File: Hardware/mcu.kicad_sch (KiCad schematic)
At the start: 20 parts, among them J1 I2C Debug, J2 Screen, J3 SPI Debug, SW1 TRIGGER, SW2 RESET, U6 ESP32-DevKitC

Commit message: Version 0.1
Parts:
- removed B1: Button, Connector_JST:JST_SH_BM04B-SRSS-TB_1x04-1MP_P1.00mm_Vertical, symbol Connector_Generic:Conn_01x03
- removed C19, C20: 104, Capacitor_SMD:C_0805_2012Metric_Pad1.18x1.45mm_HandSolder, symbol Device:C
- removed CH1: Power, Connector_JST:JST_XH_B2B-XH-A_1x02_P2.50mm_Vertical, symbol Connector_Generic:Conn_01x02
- removed D12, D2: WS2812B, LED_SMD:LED_WS2812B_PLCC4_5.0x5.0mm_P3.2mm, symbol LED:WS2812B
- removed D3: POWER LED, LED_SMD:LED_0805_2012Metric_Pad1.15x1.40mm_HandSolder, symbol Device:LED
- removed J1: I2C Debug, Connector_JST:JST_XH_B4B-XH-A_1x04_P2.50mm_Vertical, symbol Connector_Generic:Conn_01x04
- removed J2: Screen, Connector_JST:JST_XH_S8B-XH-A_1x08_P2.50mm_Horizontal, symbol Connector_Generic:Conn_01x08
- removed J3: SPI Debug, Connector_JST:JST_XH_B4B-XH-A_1x04_P2.50mm_Vertical, symbol Connector_Generic:Conn_01x04
- removed JP1: SolderJumper_2_Open, Jumper:SolderJumper-2_P1.3mm_Open_TrianglePad1.0x1.5mm, symbol Jumper:SolderJumper_2_Open
- removed JP2, JP3: SolderJumper_3_Open, Jumper:SolderJumper-3_P2.0mm_Open_TrianglePad1.0x1.5mm_NumberLabels, symbol Jumper:SolderJumper_3_Open
- removed R16: 170, Resistor_SMD:R_0805_2012Metric_Pad1.20x1.40mm_HandSolder, symbol Device:R
- removed R17: 150, Resistor_SMD:R_0805_2012Metric_Pad1.20x1.40mm_HandSolder, symbol Device:R
- removed R18, R19: 10k, Resistor_SMD:R_0805_2012Metric_Pad1.20x1.40mm_HandSolder, symbol Device:R
- removed SW1: TRIGGER, Button_Switch_THT:SW_PUSH_6mm, symbol Switch:SW_Push
- removed SW2: RESET, Button_Switch_THT:SW_PUSH_6mm, symbol Switch:SW_Push
- removed U6: ESP32-DevKitC, ESP32:ESP32-DevKitC, symbol Espressif:ESP32-DevKitC
- added D3: (no value), symbol Everlight-EAHC2835WD6:EAHC2835WD6
- added Q1: (no value), symbol Diodes_Inc._-_BSS138DW-7-F:BSS138DW-7-F
- added R10, R7, R8, R9: 10k, symbol Device:R
- added U6: (no value), symbol AS7341-DLGT:AS7341-DLGT
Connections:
- net +3V3: now also D3.1 (CATHODE), R10.1, R9.1
- net GND: now also U6.3 (GND)
- net SCL: now also Q1.6 (D2), R9.2
- net SDA: now also Q1.3 (D1), R10.2
- new net: D3.2 (ANODE), U6.4 (LDR)
- new net +1V8: Q1.2 (G2), Q1.5 (G1), R7.1, R8.1, U6.1 (VDD)
- new net SCL_2v: Q1.1 (S2), R7.2, U6.2 (SCL)
- new net SDA_2v: Q1.4 (S1), R8.2, U6.8 (SDA)
- no-connect marks 15 -> 0
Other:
- note removed: "Buttons"
- note removed: "Connectors"
- note removed: "LEDs"

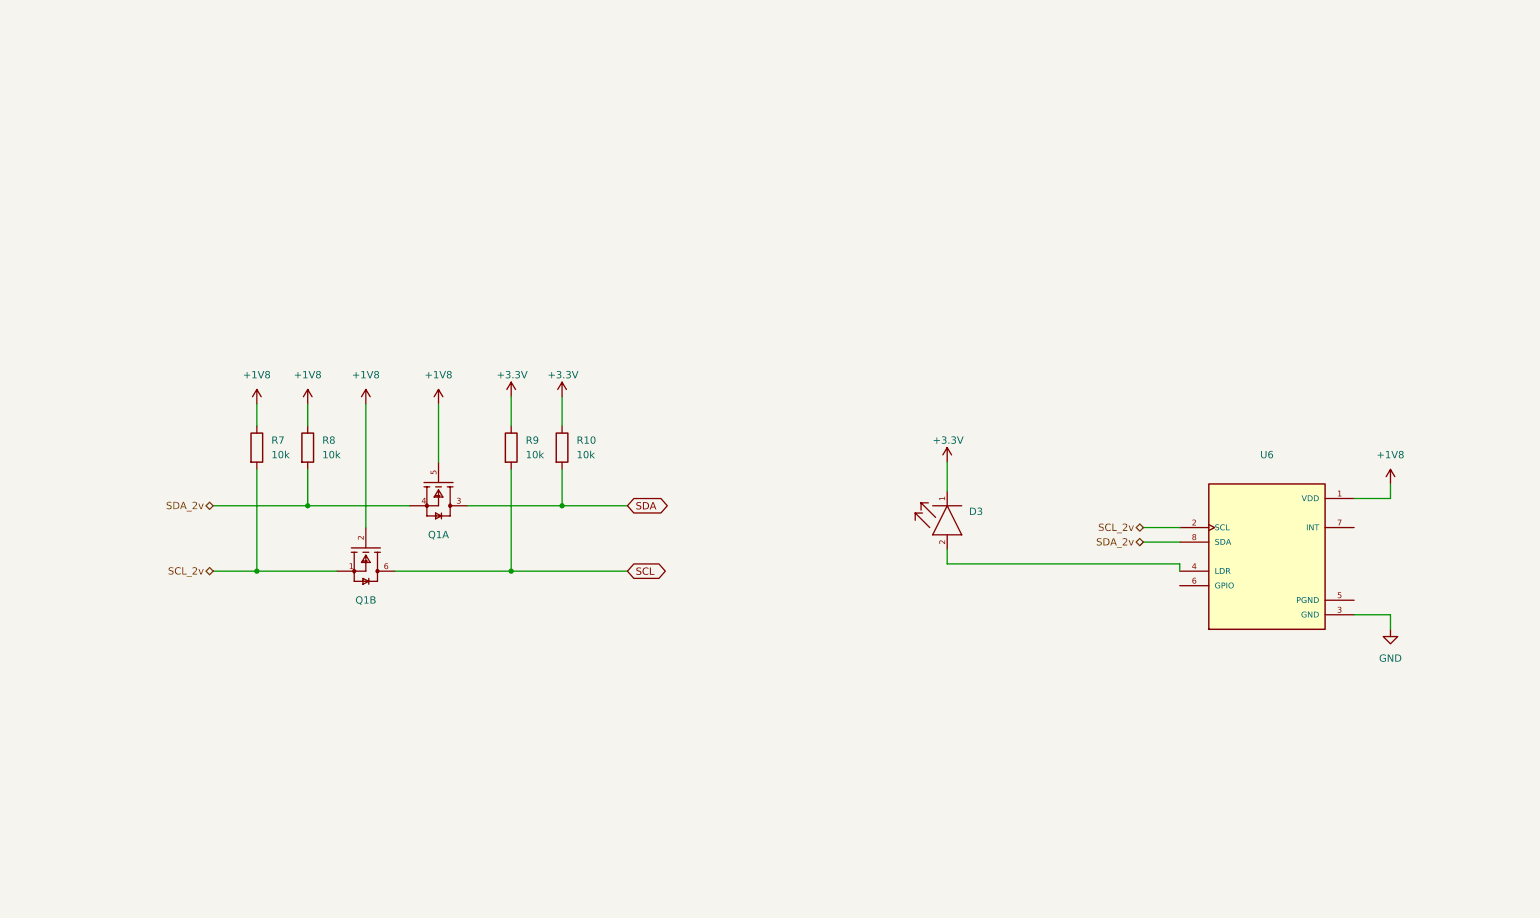
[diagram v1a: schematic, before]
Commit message: Readme + hole update
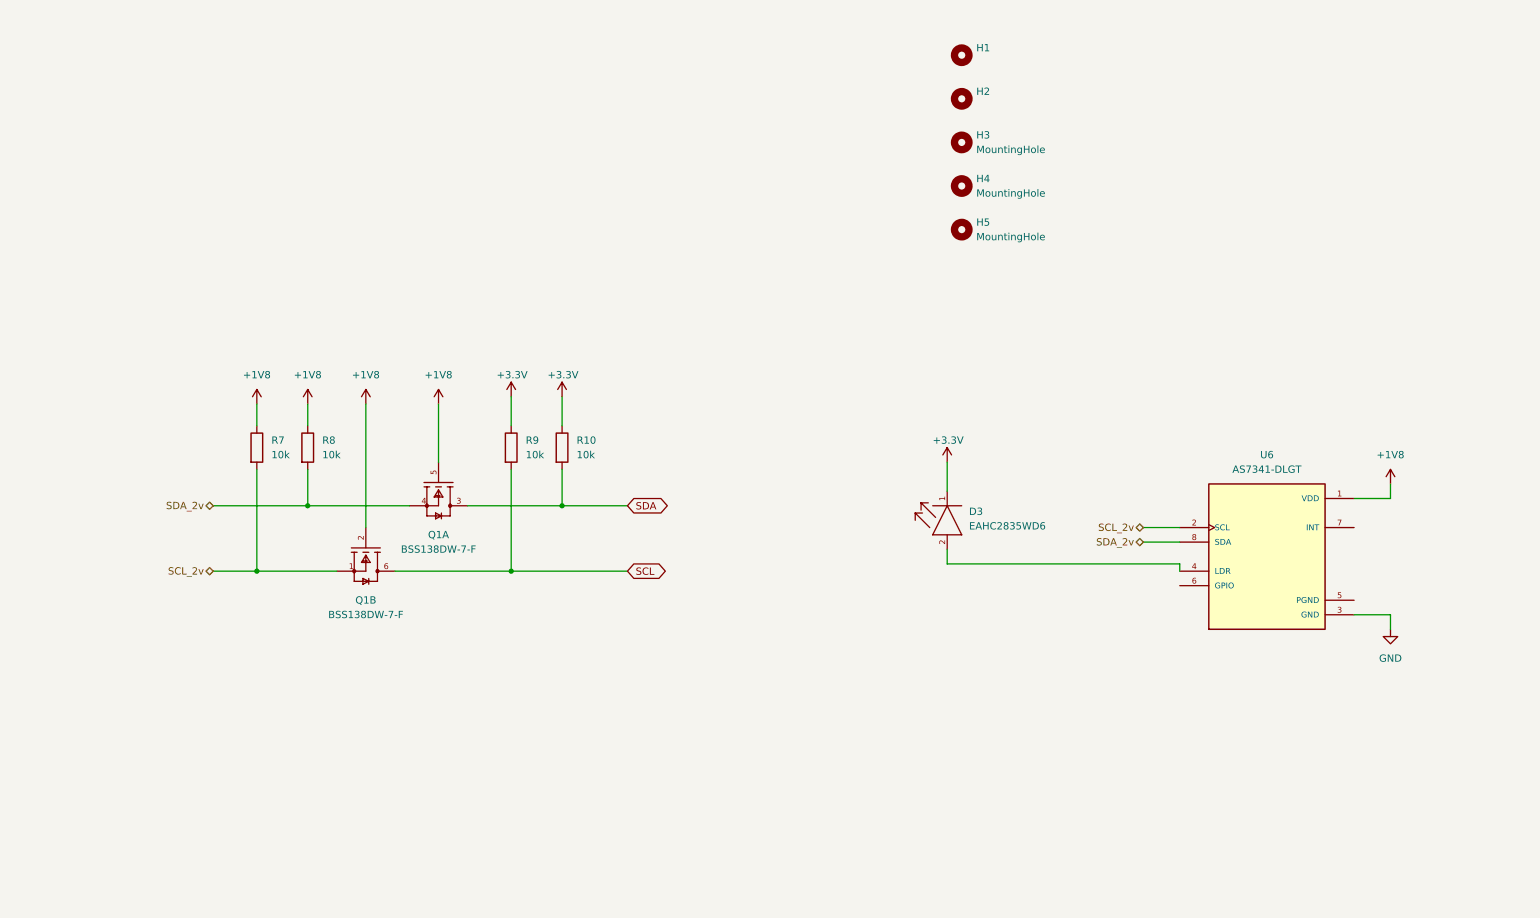
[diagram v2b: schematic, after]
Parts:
- added H1, H2: (no value), symbol Mechanical:MountingHole
- added H3, H4, H5: MountingHole, symbol Mechanical:MountingHole
- D3: value (none) -> EAHC2835WD6; footprint (none) -> Everlight-EAHC2835WD6:Everlight-EAHC2835WD6-MFG
- Q1: value (none) -> BSS138DW-7-F; footprint (none) -> BSS138DW-7-F-A:Diodes_Inc._-_BSS138DW-7-F-A
- R10, R7, R8, R9: footprint (none) -> Resistor_SMD:R_0603_1608Metric_Pad0.98x0.95mm_HandSolder
- U6: value (none) -> AS7341-DLGT; footprint (none) -> AS7341-DLGT:PSON80P310X200X110-8N
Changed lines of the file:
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@@
       (effects (font (size 1.27 1.27)) (justify left))
     )
-    (property "Footprint" "" (id 2) (at 66.802 100.33 90)
+    (property "Footprint" "Resistor_SMD:R_0603_1608Metric_Pad0.98x0.95mm_HandSolder" (id 2) (at 66.802 100.33 90)
       (effects (font (size 1.27 1.27)) hide)
     )
@@
     (pin "1")
   )
+  (symbol (lib_id "Mechanical:MountingHole") (at 182.88 39.37 0) (unit 1)
+    (in_bom yes) (on_board yes) (fields_autoplaced)
+    (property "Reference" "H2" (id 0) (at 185.42 38.0999 0)
+      (effects (font (size 1.27 1.27)) (justify left))
+    )
+    (property "Value" "" (id 1) (at 185.42 40.6399 0)
+      (effects (font (size 1.27 1.27)) (justify left))
+    )
+    (property "Footprint" "" (id 2) (at 182.88 39.37 0)
+      (effects (font (size 1.27 1.27)) hide)
+    )
+    (property "Datasheet" "~" (id 3) (at 182.88 39.37 0)
+      (effects (font (size 1.27 1.27)) hide)
+    )
+  )
   (symbol (lib_id "Everlight-EAHC2835WD6:EAHC2835WD6") (at 180.34 120.65 90) (unit 1)
     (in_bom yes) (on_board yes) (fields_autoplaced)
@@
       (effects (font (size 1.27 1.27)) (justify right))
     )
-    (property "Value" "" (id 1) (at 184.15 114.0459 90)
+    (property "Value" "EAHC2835WD6" (id 1) (at 184.15 114.0459 90)
       (effects (font (size 1.27 1.27)) (justify right))
     )
-    (property "Footprint" "" (id 2) (at 165.1 120.65 0)
+    (property "Footprint" "Everlight-EAHC2835WD6:Everlight-EAHC2835WD6-MFG" (id 2) (at 165.1 120.65 0)
       (effects (font (size 1.27 1.27)) (justify left) hide)
     )
@@
     (pin "2")
   )
+  (symbol (lib_id "Mechanical:MountingHole") (at 182.88 62.23 0) (unit 1)
+    (in_bom yes) (on_board yes) (fields_autoplaced)
+    (property "Reference" "H5" (id 0) (at 185.42 60.9599 0)
+      (effects (font (size 1.27 1.27)) (justify left))
+    )
+    (property "Value" "MountingHole" (id 1) (at 185.42 63.4999 0)
+      (effects (font (size 1.27 1.27)) (justify left))
+    )
+    (property "Footprint" "" (id 2) (at 182.88 62.23 0)
+      (effects (font (size 1.27 1.27)) hide)
+    )
+    (property "Datasheet" "~" (id 3) (at 182.88 62.23 0)
+      (effects (font (size 1.27 1.27)) hide)
+    )
+  )
   (symbol (lib_id "Device:R") (at 104.14 100.33 0) (unit 1)
     (in_bom yes) (on_board yes) (fields_autoplaced)
@@
       (effects (font (size 1.27 1.27)) (justify left))
     )
-    (property "Footprint" "" (id 2) (at 102.362 100.33 90)
+    (property "Footprint" "Resistor_SMD:R_0603_1608Metric_Pad0.98x0.95mm_HandSolder" (id 2) (at 102.362 100.33 90)
       (effects (font (size 1.27 1.27)) hide)
     )
@@
     (pin "1")
   )
+  (symbol (lib_id "Mechanical:MountingHole") (at 182.88 46.99 0) (unit 1)
+    (in_bom yes) (on_board yes) (fields_autoplaced)
+    (property "Reference" "H3" (id 0) (at 185.42 45.7199 0)
+      (effects (font (size 1.27 1.27)) (justify left))
+    )
+    (property "Value" "MountingHole" (id 1) (at 185.42 48.2599 0)
+      (effects (font (size 1.27 1.27)) (justify left))
+    )
+    (property "Footprint" "" (id 2) (at 182.88 46.99 0)
+      (effects (font (size 1.27 1.27)) hide)
+    )
+    (property "Datasheet" "~" (id 3) (at 182.88 46.99 0)
+      (effects (font (size 1.27 1.27)) hide)
+    )
+  )
   (symbol (lib_id "Diodes_Inc._-_BSS138DW-7-F:BSS138DW-7-F") (at 91.44 100.33 270) (unit 1)
     (in_bom yes) (on_board yes) (fields_autoplaced)
     (property "Reference" "Q1" (id 0) (at 91.44 115.57 90))
-    (property "Value" "" (id 1) (at 91.44 118.11 90))
-    (property "Footprint" "" (id 2) (at 104.14 100.33 0)
+    (property "Value" "BSS138DW-7-F" (id 1) (at 91.44 118.11 90))
+    (property "Footprint" "BSS138DW-7-F-A:Diodes_Inc._-_BSS138DW-7-F-A" (id 2) (at 104.14 100.33 0)
       (effects (font (size 1.27 1.27)) (justify left) hide)
     )
@@
       (effects (font (size 1.27 1.27)) (justify left))
     )
-    (property "Footprint" "" (id 2) (at 111.252 100.33 90)
+    (property "Footprint" "Resistor_SMD:R_0603_1608Metric_Pad0.98x0.95mm_HandSolder" (id 2) (at 111.252 100.33 90)
       (effects (font (size 1.27 1.27)) hide)
     )
@@
       (effects (font (size 1.27 1.27)) (justify left))
     )
-    (property "Footprint" "" (id 2) (at 57.912 100.33 90)
+    (property "Footprint" "Resistor_SMD:R_0603_1608Metric_Pad0.98x0.95mm_HandSolder" (id 2) (at 57.912 100.33 90)
       (effects (font (size 1.27 1.27)) hide)
     )
@@
     (pin "2")
   )
+  (symbol (lib_id "Mechanical:MountingHole") (at 182.88 54.61 0) (unit 1)
+    (in_bom yes) (on_board yes) (fields_autoplaced)
+    (property "Reference" "H4" (id 0) (at 185.42 53.3399 0)
+      (effects (font (size 1.27 1.27)) (justify left))
+    )
+    (property "Value" "MountingHole" (id 1) (at 185.42 55.8799 0)
+      (effects (font (size 1.27 1.27)) (justify left))
+    )
+    (property "Footprint" "" (id 2) (at 182.88 54.61 0)
+      (effects (font (size 1.27 1.27)) hide)
+    )
+    (property "Datasheet" "~" (id 3) (at 182.88 54.61 0)
+      (effects (font (size 1.27 1.27)) hide)
+    )
+  )
   (symbol (lib_id "AS7341-DLGT:AS7341-DLGT") (at 236.22 119.38 0) (unit 1)
     (in_bom yes) (on_board yes) (fields_autoplaced)
     (property "Reference" "U6" (id 0) (at 236.22 101.6 0))
-    (property "Value" "" (id 1) (at 236.22 104.14 0))
-    (property "Footprint" "" (id 2) (at 236.22 119.38 0)
+    (property "Value" "AS7341-DLGT" (id 1) (at 236.22 104.14 0))
+    (property "Footprint" "AS7341-DLGT:PSON80P310X200X110-8N" (id 2) (at 236.22 119.38 0)
       (effects (font (size 1.27 1.27)) (justify left bottom) hide)
     )
@@
     (pin "8")
   )
+  (symbol (lib_id "Mechanical:MountingHole") (at 182.88 31.75 0) (unit 1)
+    (in_bom yes) (on_board yes) (fields_autoplaced)
+    (property "Reference" "H1" (id 0) (at 185.42 30.4799 0)
+      (effects (font (size 1.27 1.27)) (justify left))
+    )
+    (property "Value" "" (id 1) (at 185.42 33.0199 0)
+      (effects (font (size 1.27 1.27)) (justify left))
+    )
+    (property "Footprint" "" (id 2) (at 182.88 31.75 0)
+      (effects (font (size 1.27 1.27)) hide)
+    )
+    (property "Datasheet" "~" (id 3) (at 182.88 31.75 0)
+      (effects (font (size 1.27 1.27)) hide)
+    )
+  )
   (symbol (lib_id "power:+1V8") (at 257.81 106.68 0) (unit 1)
     (in_bom yes) (on_board yes) (fields_autoplaced)
@@
     (in_bom yes) (on_board yes) (fields_autoplaced)
     (property "Reference" "Q1" (id 0) (at 78.74 127 90))
-    (property "Value" "" (id 1) (at 78.74 129.54 90))
-    (property "Footprint" "" (id 2) (at 91.44 111.76 0)
-      (effects (font (size 1.27 1.27)) (justify left) hide)
-    )
+    (property "Value" "BSS138DW-7-F" (id 1) (at 78.74 129.54 90))
+    (property "Footprint" "BSS138DW-7-F-A:Diodes_Inc._-_BSS138DW-7-F-A" (id 2) (at 91.44 111.76 0)
+      (effects (font (size 1.27 1.27)) (justify left) hide)
+    )

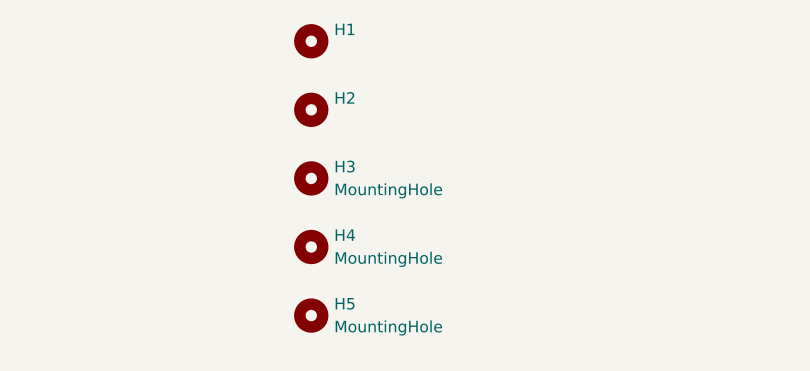
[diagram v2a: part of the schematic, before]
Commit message: Added hole placement measurements
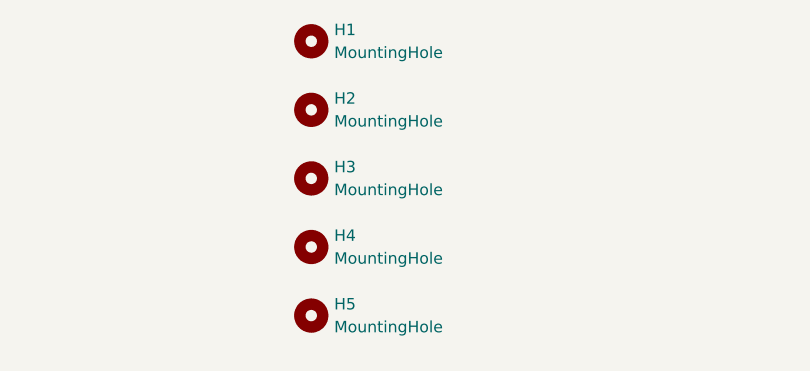
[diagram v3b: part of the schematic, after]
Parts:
- H1, H2: value (none) -> MountingHole; footprint (none) -> MountingHole:MountingHole_2.2mm_M2_ISO7380_Pad
- H3, H4, H5: footprint (none) -> MountingHole:MountingHole_2.2mm_M2_ISO7380_Pad
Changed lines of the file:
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@@
       (effects (font (size 1.27 1.27)) (justify left))
     )
-    (property "Value" "" (id 1) (at 185.42 40.6399 0)
-      (effects (font (size 1.27 1.27)) (justify left))
-    )
-    (property "Footprint" "" (id 2) (at 182.88 39.37 0)
+    (property "Value" "MountingHole" (id 1) (at 185.42 40.6399 0)
+      (effects (font (size 1.27 1.27)) (justify left))
+    )
+    (property "Footprint" "MountingHole:MountingHole_2.2mm_M2_ISO7380_Pad" (id 2) (at 182.88 39.37 0)
       (effects (font (size 1.27 1.27)) hide)
     )
@@
       (effects (font (size 1.27 1.27)) (justify left))
     )
-    (property "Footprint" "" (id 2) (at 182.88 62.23 0)
+    (property "Footprint" "MountingHole:MountingHole_2.2mm_M2_ISO7380_Pad" (id 2) (at 182.88 62.23 0)
       (effects (font (size 1.27 1.27)) hide)
     )
@@
       (effects (font (size 1.27 1.27)) (justify left))
     )
-    (property "Footprint" "" (id 2) (at 182.88 46.99 0)
+    (property "Footprint" "MountingHole:MountingHole_2.2mm_M2_ISO7380_Pad" (id 2) (at 182.88 46.99 0)
       (effects (font (size 1.27 1.27)) hide)
     )
@@
       (effects (font (size 1.27 1.27)) (justify left))
     )
-    (property "Footprint" "" (id 2) (at 182.88 54.61 0)
+    (property "Footprint" "MountingHole:MountingHole_2.2mm_M2_ISO7380_Pad" (id 2) (at 182.88 54.61 0)
       (effects (font (size 1.27 1.27)) hide)
     )
@@
       (effects (font (size 1.27 1.27)) (justify left))
     )
-    (property "Value" "" (id 1) (at 185.42 33.0199 0)
-      (effects (font (size 1.27 1.27)) (justify left))
-    )
-    (property "Footprint" "" (id 2) (at 182.88 31.75 0)
-      (effects (font (size 1.27 1.27)) hide)
-    )
+    (property "Value" "MountingHole" (id 1) (at 185.42 33.0199 0)
+      (effects (font (size 1.27 1.27)) (justify left))
+    )
+    (property "Footprint" "MountingHole:MountingHole_2.2mm_M2_ISO7380_Pad" (id 2) (at 182.88 31.75 0)
+      (effects (font (size 1.27 1.27)) hide)
+    )

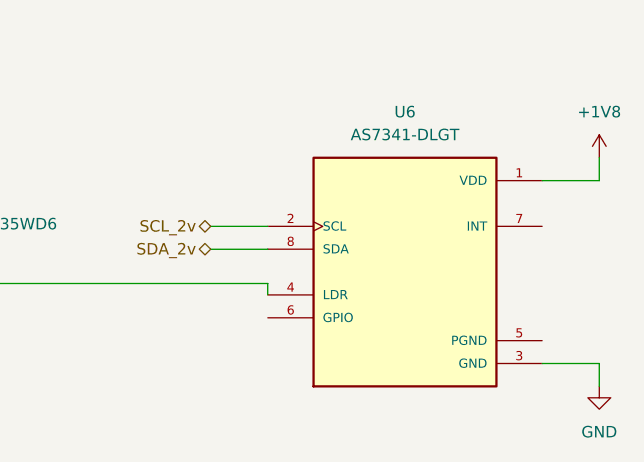
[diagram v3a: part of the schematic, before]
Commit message: removed TP561023, added footprint libraries
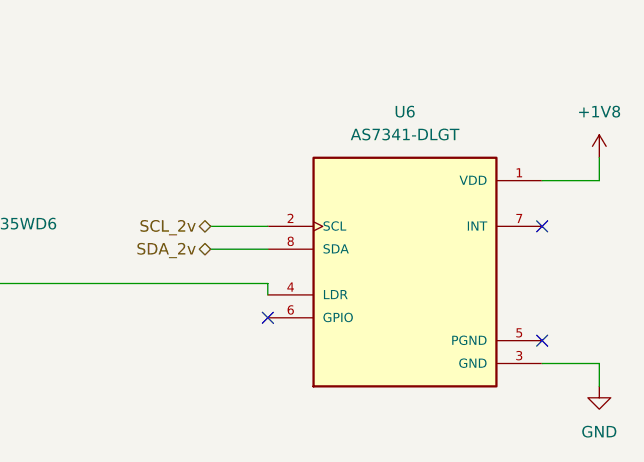
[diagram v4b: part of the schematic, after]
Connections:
- no-connect marks 0 -> 3
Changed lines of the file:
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@@
   (junction (at 68.58 110.49) (diameter 0) (color 0 0 0 0)
   )
+  (no_connect (at 251.46 114.3))
+  (no_connect (at 220.98 124.46))
+  (no_connect (at 251.46 127))
   (wire (pts (xy 220.98 120.65) (xy 220.98 121.92))
     (stroke (width 0) (type default) (color 0 0 0 0))

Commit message: Updated from discord feedback
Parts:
- removed R10, R9: 10k, Resistor_SMD:R_0603_1608Metric_Pad0.98x0.95mm_HandSolder, symbol Device:R
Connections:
- net +3V3: now also D3.2 (ANODE); no longer D3.1 (CATHODE)
- net GND: now also U6.5 (PGND)
- net at U6.4 (LDR): now also D3.1 (CATHODE); no longer D3.2 (ANODE)
- no-connect marks 3 -> 2
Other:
- moved on the sheet: D3
